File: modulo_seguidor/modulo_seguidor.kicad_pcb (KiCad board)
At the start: 2 copper layers, 150 x 76 mm, 26 parts, among them J1 Battery, J6 puerto sensores, M1 Motor_IZQ, M2 Motor_DER, SW1 SW_Push, SW2 SW_Nidec_CAS-120A1, U1 LM7806_TO220, U2 L298N

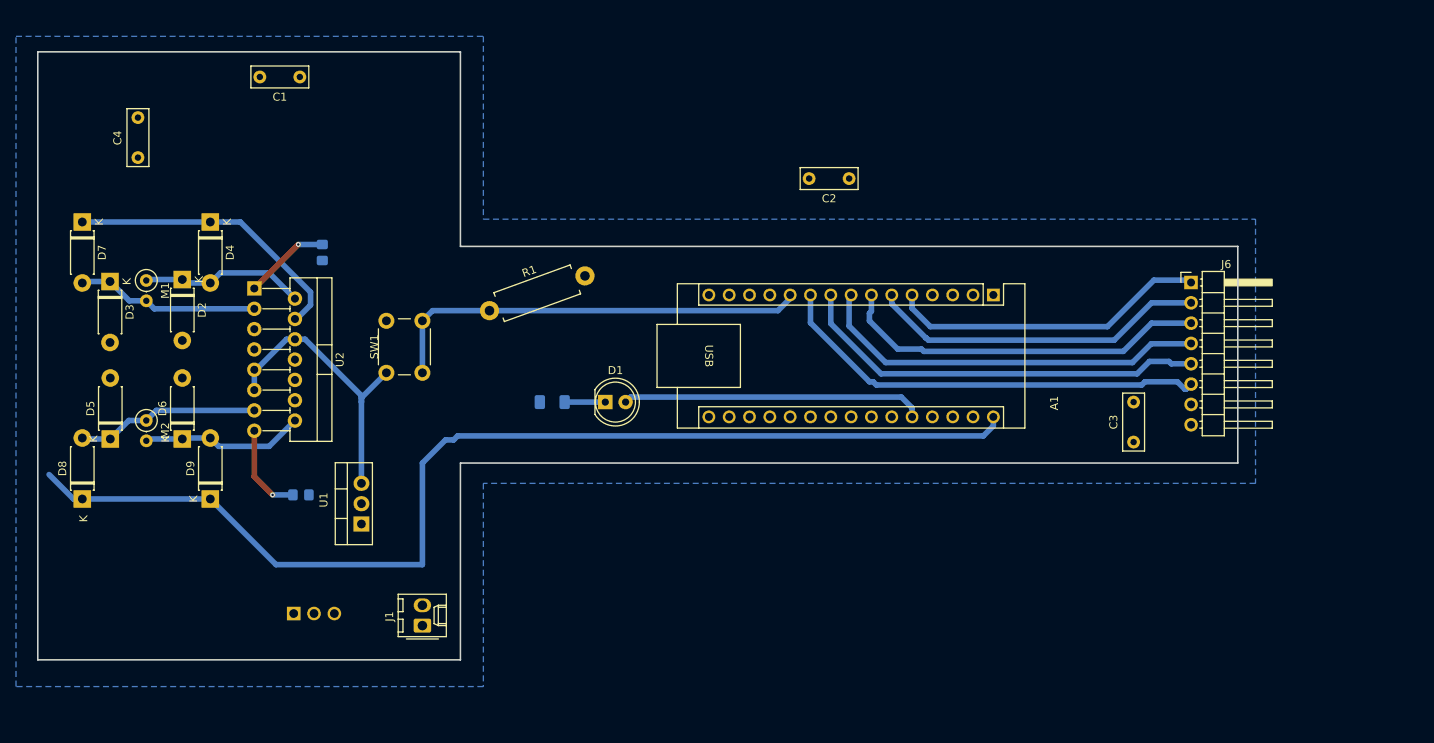
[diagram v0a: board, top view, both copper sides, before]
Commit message: Placa PH - Huellas y ubicaciones
Cambie las ubicaciones de los pines del arduino que dan a los motores para mejor ubicación
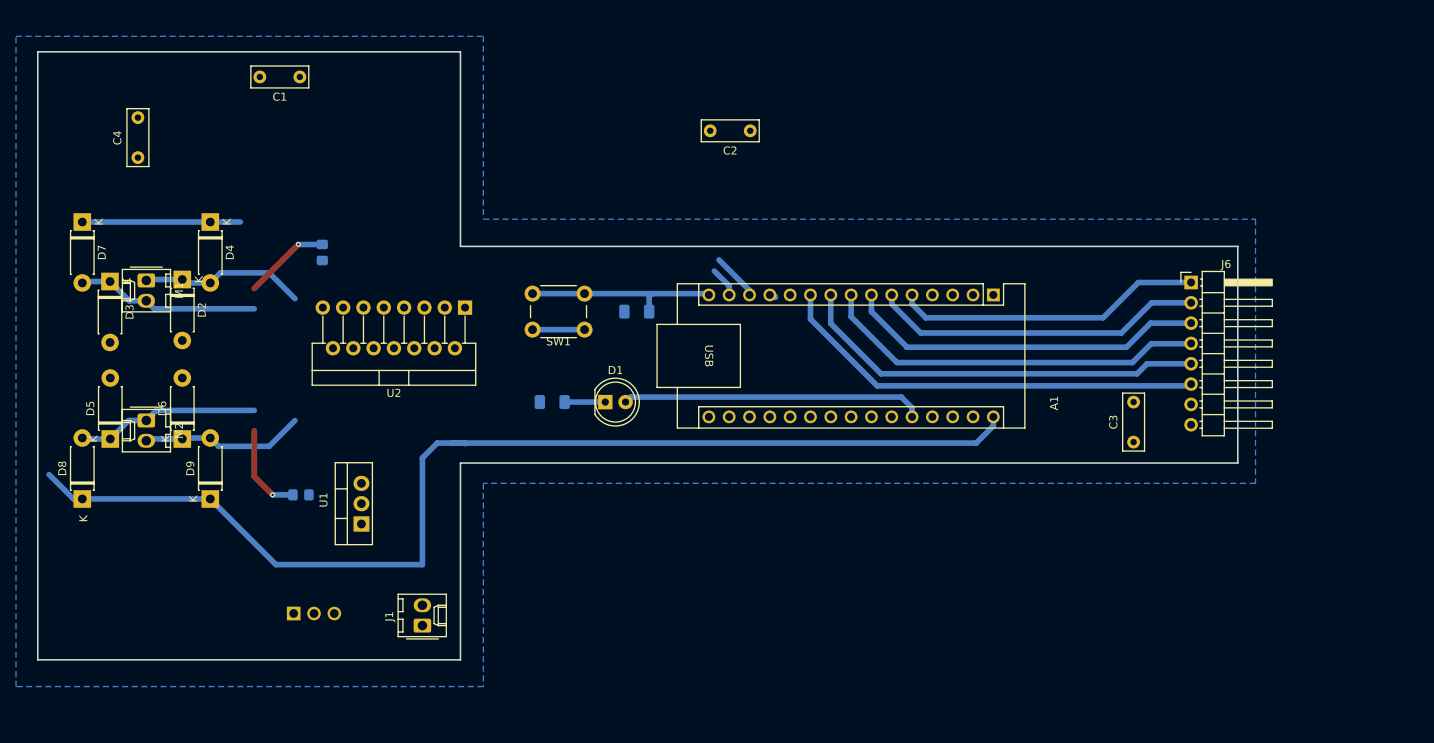
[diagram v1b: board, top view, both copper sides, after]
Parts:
- M1, M2: footprint Resistor_THT:R_Axial_DIN0207_L6.3mm_D2.5mm_P2.54mm_Vertical -> Connector_Molex:Molex_KK-254_AE-6410-02A_1x02_P2.54mm_Vertical
- R1: footprint Resistor_THT:R_Axial_DIN0411_L9.9mm_D3.6mm_P12.70mm_Horizontal -> Resistor_SMD:R_1206_3216Metric_Pad1.30x1.75mm_HandSolder; moved to B.Cu
- moved U2 26.5 mm to (119.6, 94.9), turned to 180 degrees
- moved SW1 25.3 mm to (134.6, 97.6), turned to 180 degrees
- moved R1 18.4 mm to (141.1, 95.4), turned to 180 degrees
- moved C2 13.7 mm to (155.3, 72.8)
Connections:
- A1 pad 11: /Boton_encendido -> /Entrada DIG Motor B
- A1 pad 12: /Entrada PWM Motor A -> /Entrada PWM Motor B
- A1 pad 14: /Entrada DIG Motor B -> /Entrada PWM Motor A
- A1 pad 15: /Entrada PWM Motor B -> /Boton_encendido
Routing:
- net /Boton_encendido: track 54.8 -> 24.5 mm
- net Salida Regulador: track 36.3 -> 6.50 mm
- net VCC: track 174.9 -> 161.0 mm
- net /Entrada DIG Motor A: track 0.00 -> 5.97 mm
- net /Entrada PWM Motor A: track 0.00 -> 3.76 mm
- net /Sensor1: track 40.0 -> 38.5 mm
- net /Sensor3: track 46.6 -> 45.1 mm
- net /Sensor4: track 49.6 -> 48.5 mm
- net /Entrada PWM Motor B: track 0.00 -> 0.86 mm
- net /Sensor6: track 55.1 -> 54.3 mm
- net /Sensor2: track 42.3 -> 41.6 mm

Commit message: feat(Modulo_seguidor) "Diseño con todo conectado + detalles"
Cambie de lugar algunos pines del arduino para mejor llega a las conexiones . Entre ellos :
- Botón Encendido del D15 al D16
- Encender Botón: de A7 a A1
- Se deja un especio en el medio donde iría apoyada la batería
-  Las conexiones rojas indican que por arriba se pasará un cable

Propuesta: Si bien llegué a conectar la salida del regulador a la placa de sensores. Capaz sería conveniente alimentar esa placa con los 5V del arduino
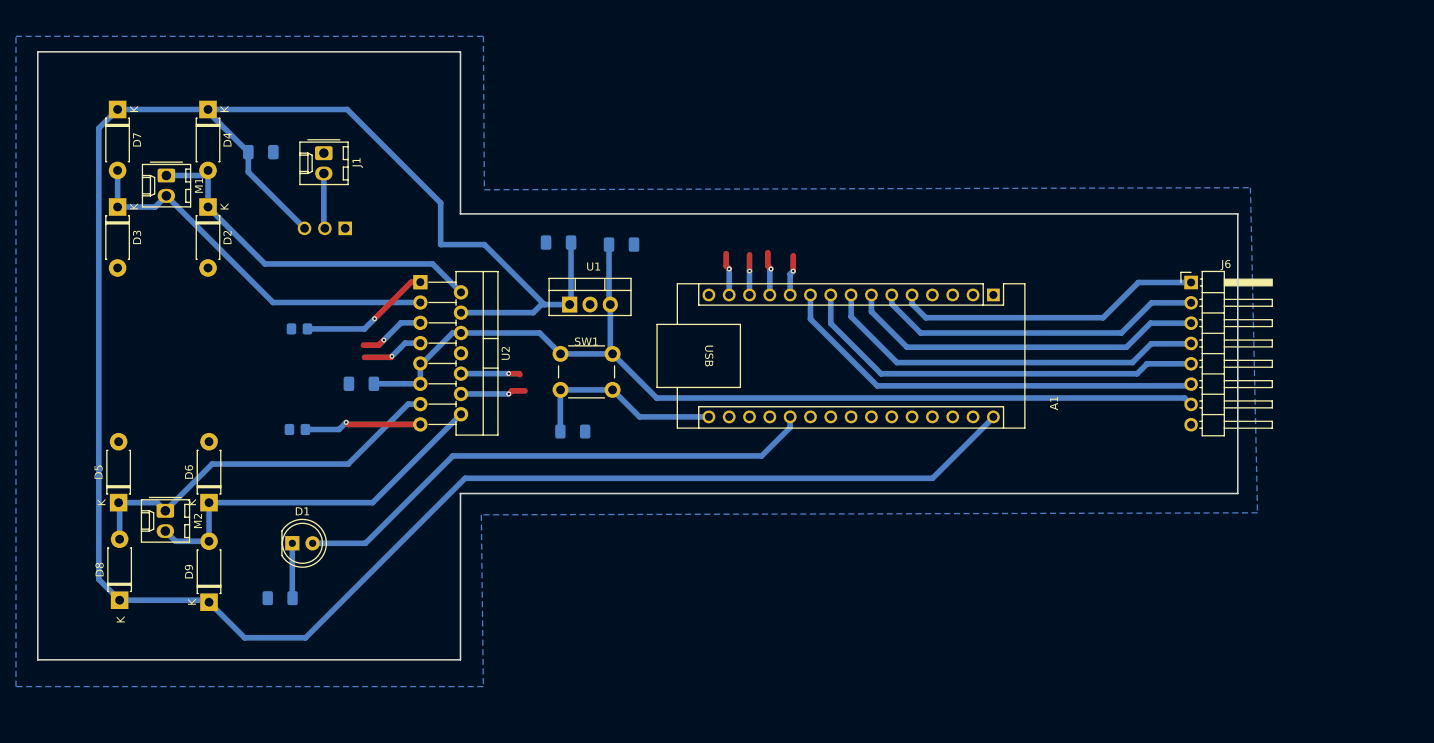
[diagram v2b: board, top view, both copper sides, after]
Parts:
- C1, C2, C3, C4: footprint Capacitor_THT:C_Disc_D7.0mm_W2.5mm_P5.00mm -> Capacitor_SMD:C_1206_3216Metric_Pad1.33x1.80mm_HandSolder; moved to B.Cu
- moved C3 96.8 mm to (106.7, 104.4), turned to 0 degrees
- moved J1 60.3 mm to (102.0, 75.6), turned to -90 degrees
- moved C4 53.6 mm to (131.3, 86.7), turned to 0 degrees
- moved SW2 48.6 mm to (104.6, 85.0), turned to 90 degrees
- moved D1 42.9 mm to (98.0, 124.3)
- moved R2 41.9 mm to (96.5, 131.2)
- moved U1 37.8 mm to (132.7, 94.5), turned to 0 degrees
- moved C2 21.5 mm to (139.2, 87.0), turned to 0 degrees
- moved R1 17.0 mm to (133.1, 110.4), turned to 0 degrees
- moved D7 14.7 mm to (76.2, 70.1)
- moved D4 14.1 mm to (87.5, 70.1)
- moved D8 13.5 mm to (76.5, 131.4)
- moved M1 13.4 mm to (82.3, 78.4)
- moved D9 12.9 mm to (87.6, 131.7)
- moved M2 11.5 mm to (82.2, 120.3)
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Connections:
- A1 pad 15: /Boton_encendido -> unconnected-(A1-D12-Pad15)
- A1 pad 16: unconnected-(A1-D13-Pad16) -> /Boton_encendido
- A1 pad 20: unconnected-(A1-A1-Pad20) -> Net-(A1-A1)
- A1 pad 26: Net-(A1-A7) -> unconnected-(A1-A7-Pad26)
- D1 pad 2: Net-(A1-A7) -> Net-(A1-A1)
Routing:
- net VCC: track 161.0 -> 294.2 mm
- net Salida Regulador: track 6.50 -> 123.8 mm
- net Net-(A1-A1): track 0.00 -> 67.0 mm
- net Net-(A1-A7): track 37.8 -> 0.00 mm
- net Net-(D6-K): track 20.5 -> 46.9 mm
- net Net-(D3-K): track 23.0 -> 48.7 mm
- net Net-(D5-K): track 23.0 -> 48.5 mm
- net Net-(D2-K): track 20.7 -> 46.1 mm
- net /Entrada DIG Motor B: track 0.00 -> 13.2 mm, vias 0 -> 2
- net /Entrada PWM Motor B: track 0.86 -> 12.9 mm, vias 0 -> 2
- net /Entrada PWM Motor A: track 3.76 -> 13.6 mm, vias 0 -> 2
- net Net-(J1-Pin_2): track 0.00 -> 6.91 mm
- net /Entrada DIG Motor A: track 5.97 -> 12.7 mm, vias 0 -> 2
- net Net-(U2-SENSE_A): track 10.8 -> 16.5 mm
- net Net-(U2-SENSE_B): track 11.5 -> 14.8 mm
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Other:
- outline, holes or cut-outs redrawn

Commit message: Update modulo_seguidor.kicad_pcb
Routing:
- net VCC: track 294.2 -> 291.0 mm
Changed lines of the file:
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@@
+	)
+	(segment
+		(start 73.853608 72.450392)
+		(end 73.853608 128.844608)
+		(width 0.7)
+		(layer "B.Cu")
+		(net 1)
+	)
+	(segment
+		(start 132.8805 86.741)
+		(end 132.8805 94.3225)
+		(width 0.7)
+		(layer "B.Cu")
+		(net 1)
+	)
+	(segment
+		(start 97.917 136.144)
+		(end 92.075 136.144)
+		(width 0.7)
+		(layer "B.Cu")
+		(net 1)
+	)
+	(segment
+		(start 129.183504 94.488)
+		(end 129.54 94.488)
+		(width 0.7)
+		(layer "B.Cu")
+		(net 1)
+	)
+	(segment
+		(start 87.503 70.3965)
+		(end 92.5445 75.438)
+		(width 0.7)
+		(layer "B.Cu")
+		(net 1)
+	)
+	(segment
+		(start 92.5445 77.9395)
+		(end 99.568 84.963)
+		(width 0.7)
+		(layer "B.Cu")
+		(net 1)
+	)
+	(segment
+		(start 116.205 85.471)
+		(end 126.238 95.504)
+		(width 0.7)
+		(layer "B.Cu")
+		(net 1)
+	)
+	(segment
+		(start 87.503 70.104)
+		(end 105.156 70.104)
+		(width 0.7)
+		(layer "B.Cu")
+		(net 1)
+	)
+	(segment
+		(start 87.376 131.445)
+		(end 87.63 131.699)
+		(width 0.7)
+		(layer "B.Cu")
+		(net 1)
+	)
+	(segment
+		(start 126.238 95.504)
+		(end 128.167504 95.504)
+		(width 0.7)
+		(layer "B.Cu")
+		(net 1)
 	)
 	(segment
@@
 	)
 	(segment
-		(start 73.853608 72.450392)
-		(end 73.853608 128.844608)
-		(width 0.7)
-		(layer "B.Cu")
-		(net 1)
-	)
-	(segment
-		(start 116.586 81.788)
-		(end 116.586 86.995)
-		(width 0.7)
-		(layer "B.Cu")
-		(net 1)
-	)
-	(segment
-		(start 132.8805 86.741)
-		(end 132.8805 94.3225)
-		(width 0.7)
-		(layer "B.Cu")
-		(net 1)
-	)
-	(segment
-		(start 185.669994 108.60771)
-		(end 178.072704 116.205)
-		(width 0.7)
-		(layer "B.Cu")
-		(net 1)
-	)
-	(segment
-		(start 129.183504 94.488)
-		(end 129.54 94.488)
-		(width 0.7)
-		(layer "B.Cu")
-		(net 1)
-	)
-	(segment
-		(start 87.503 70.3965)
-		(end 92.5445 75.438)
-		(width 0.7)
-		(layer "B.Cu")
-		(net 1)
-	)
-	(segment
-		(start 92.5445 77.9395)
-		(end 99.568 84.963)
-		(width 0.7)
-		(layer "B.Cu")
-		(net 1)
-	)
-	(segment
-		(start 104.902 70.104)
-		(end 116.586 81.788)
-		(width 0.7)
-		(layer "B.Cu")
-		(net 1)
-	)
-	(segment
-		(start 87.376 131.445)
-		(end 87.63 131.699)
-		(width 0.7)
-		(layer "B.Cu")
-		(net 1)
-	)
-	(segment
 		(start 129.54 94.488)
 		(end 132.715 94.488)
@@
 	)
 	(segment
-		(start 122.047 86.995)
-		(end 129.54 94.488)
-		(width 0.7)
-		(layer "B.Cu")
-		(net 1)
-	)
-	(segment
-		(start 119.634 116.205)
-		(end 99.695 136.144)
+		(start 185.669994 108.60771)
+		(end 178.707704 115.57)
+		(width 0.7)
+		(layer "B.Cu")
+		(net 1)
+	)
+	(segment
+		(start 105.156 70.104)
+		(end 116.205 81.153)
 		(width 0.7)
 		(layer "B.Cu")
@@
 	)
 	(segment
-		(start 178.072704 116.205)
-		(end 119.634 116.205)
-		(width 0.7)
-		(layer "B.Cu")
-		(net 1)
-	)
-	(segment
-		(start 116.586 86.995)
-		(end 122.047 86.995)
-		(width 0.7)
-		(layer "B.Cu")
-		(net 1)
-	)
-	(segment
-		(start 87.503 70.104)
-		(end 104.902 70.104)
+		(start 178.707704 115.57)
+		(end 118.491 115.57)
+		(width 0.7)
+		(layer "B.Cu")
+		(net 1)
+	)
+	(segment
+		(start 92.075 136.144)
+		(end 87.63 131.699)
 		(width 0.7)
 		(layer "B.Cu")
@@
 	)
 	(segment
-		(start 99.695 136.144)
-		(end 92.075 136.144)
+		(start 87.503 70.104)
+		(end 87.63 69.977)
 		(width 0.7)
 		(layer "B.Cu")
@@
 	(segment
 		(start 119.126 95.504)
-		(end 128.167504 95.504)
+		(end 126.238 95.504)
 		(width 0.7)
 		(layer "B.Cu")
@@
 	)
 	(segment
+		(start 118.491 115.57)
+		(end 97.917 136.144)
+		(width 0.7)
+		(layer "B.Cu")
+		(net 1)
+	)
+	(segment
 		(start 76.2 70.104)
 		(end 73.853608 72.450392)
@@
 	)
 	(segment
-		(start 92.075 136.144)
-		(end 87.63 131.699)
-		(width 0.7)
-		(layer "B.Cu")
-		(net 1)
-	)
-	(segment
 		(start 92.5445 75.438)
 		(end 92.5445 77.9395)
+		(width 0.7)
+		(layer "B.Cu")
+		(net 1)
+	)
+	(segment
+		(start 116.205 81.153)
+		(end 116.205 85.471)
 		(width 0.7)
 		(layer "B.Cu")
@@
 	)
 	(segment
-		(start 107.188 124.333)
-		(end 118.11 113.411)
+		(start 157.353 112.776)
+		(end 160.269994 109.859006)
 		(width 0.7)
 		(layer "B.Cu")
@@
 	)
 	(segment
-		(start 118.11 113.411)
-		(end 156.718 113.411)
+		(start 100.579 124.333)
+		(end 106.426 124.333)
 		(width 0.7)
 		(layer "B.Cu")
@@
 	)
 	(segment
-		(start 100.579 124.333)
-		(end 107.188 124.333)
+		(start 117.983 112.776)
+		(end 157.353 112.776)
 		(width 0.7)
 		(layer "B.Cu")
@@
 	)
 	(segment
-		(start 156.718 113.411)
-		(end 160.269994 109.859006)
-		(width 0.7)
-		(layer "B.Cu")
+		(start 106.426 124.333)
+		(end 117.983 112.776)
+		(width 0.7)
+		(layer "B.Cu")

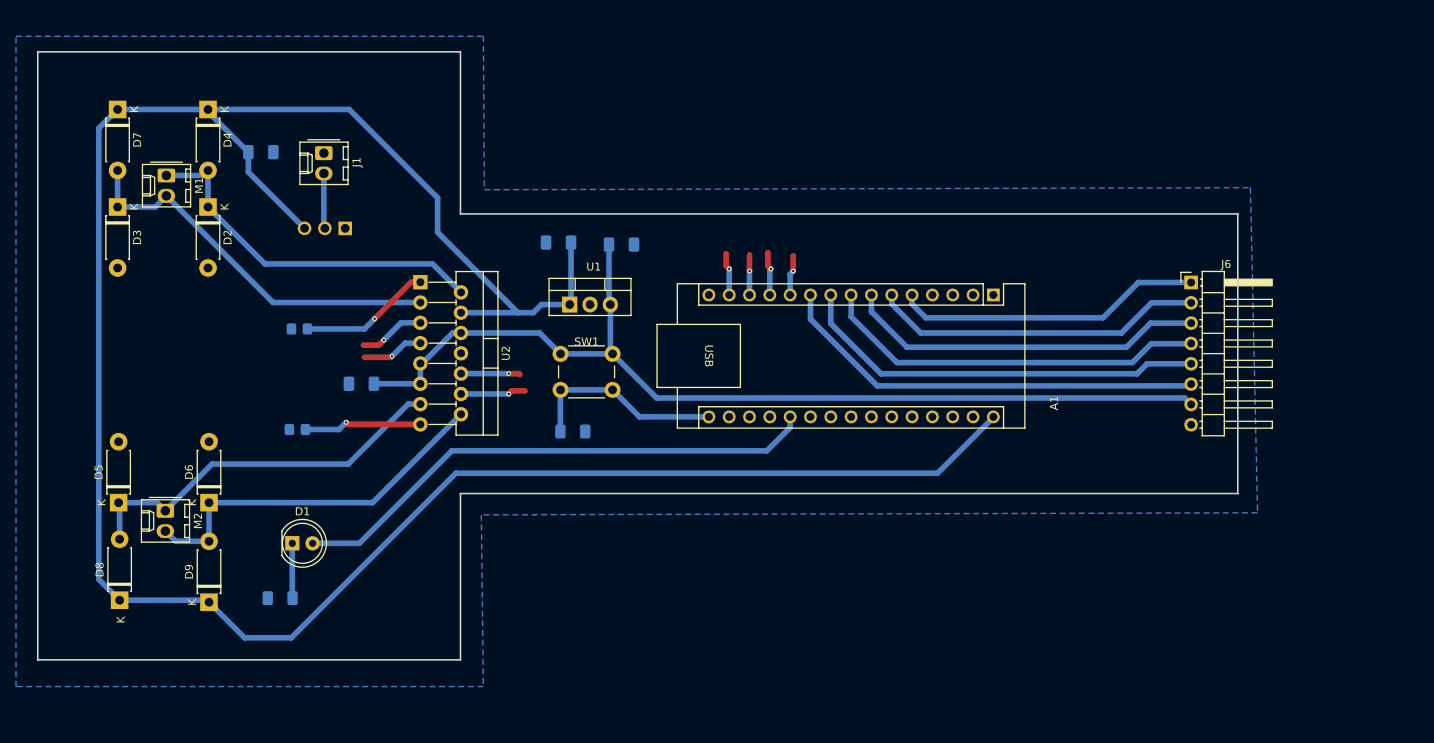
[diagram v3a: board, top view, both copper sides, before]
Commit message: refactor(modulo-seguidor): Redistribución y cambio de entrada del puente por housing
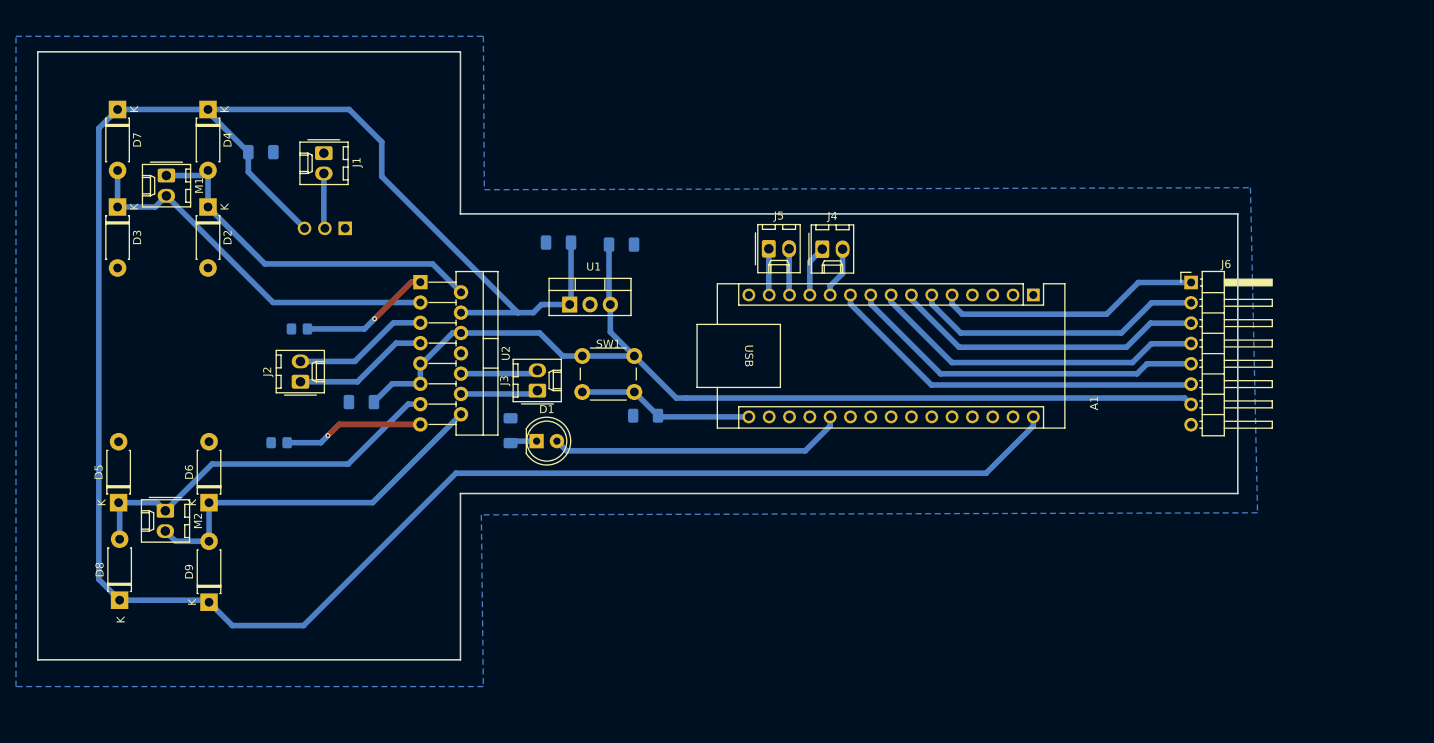
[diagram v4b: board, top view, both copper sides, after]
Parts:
- added J2: Motor A Entradas, Connector_Molex:Molex_KK-254_AE-6410-02A_1x02_P2.54mm_Vertical, F.Cu at (99.1, 104.1)
- added J3: Motor B Entradas, Connector_Molex:Molex_KK-254_AE-6410-02A_1x02_P2.54mm_Vertical, F.Cu at (128.7, 105.2)
- added J4: Motor A Salidas, Connector_Molex:Molex_KK-254_AE-6410-02A_1x02_P2.54mm_Vertical, F.Cu at (164.3, 87.6)
- added J5: Motor B Salidas, Connector_Molex:Molex_KK-254_AE-6410-02A_1x02_P2.54mm_Vertical, F.Cu at (157.6, 87.5)
- moved R2 35.6 mm to (125.3, 110.3), turned to 90 degrees
- moved D1 33.1 mm to (128.6, 111.6)
- moved R1 9.32 mm to (142.2, 108.4), turned to 180 degrees
- moved A1 5.00 mm to (190.7, 93.3)
- moved R4 2.82 mm to (96.4, 111.8)
- moved SW1 2.73 mm to (134.3, 100.9)
- moved C3 2.29 mm to (106.7, 106.7)
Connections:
- A1 pad 11: /Entrada DIG Motor B -> Net-(A1-D8)
- A1 pad 12: /Entrada PWM Motor B -> Net-(A1-D9)
- A1 pad 13: /Entrada DIG Motor A -> Net-(A1-D10)
- A1 pad 14: /Entrada PWM Motor A -> Net-(A1-D11)
- U2 pad 10: /Entrada PWM Motor B -> Net-(J3-Pin_2)
- U2 pad 12: /Entrada DIG Motor B -> Net-(J3-Pin_1)
- U2 pad 5: /Entrada PWM Motor A -> Net-(J2-Pin_2)
- U2 pad 7: /Entrada DIG Motor A -> Net-(J2-Pin_1)
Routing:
- net Net-(A1-A1): track 67.0 -> 37.1 mm
- net Net-(J2-Pin_1): track 0.00 -> 17.0 mm
- net Net-(J2-Pin_2): track 0.00 -> 17.0 mm
- net /Entrada PWM Motor A: track 13.6 -> 0.00 mm, vias 2 -> 0
- net /Entrada DIG Motor B: track 13.2 -> 0.00 mm, vias 2 -> 0
- net /Entrada PWM Motor B: track 12.9 -> 0.00 mm, vias 2 -> 0
- net /Entrada DIG Motor A: track 12.7 -> 0.00 mm, vias 2 -> 0
- net Net-(J3-Pin_1): track 0.00 -> 9.72 mm
- net Net-(J3-Pin_2): track 0.00 -> 9.72 mm
- net /Sensor5: track 51.7 -> 45.3 mm
- net Net-(A1-D8): track 0.00 -> 6.37 mm
- net Net-(A1-D9): track 0.00 -> 6.37 mm
- net /Sensor4: track 48.5 -> 42.4 mm
- net /Sensor3: track 45.1 -> 39.2 mm
- net /Sensor6: track 54.3 -> 48.4 mm
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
